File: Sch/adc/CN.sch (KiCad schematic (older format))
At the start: 20 parts, among them J1 JP4, J2 Header5, P1 CONN_02X40, U1 LTC2292

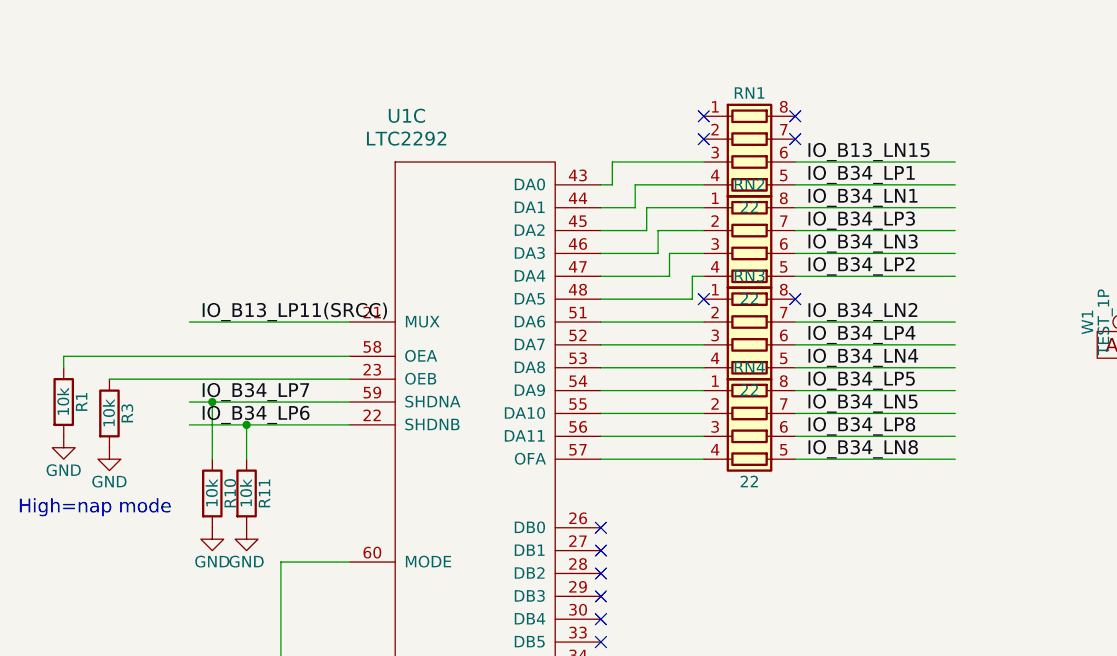
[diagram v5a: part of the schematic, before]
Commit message: Fix RA footprint
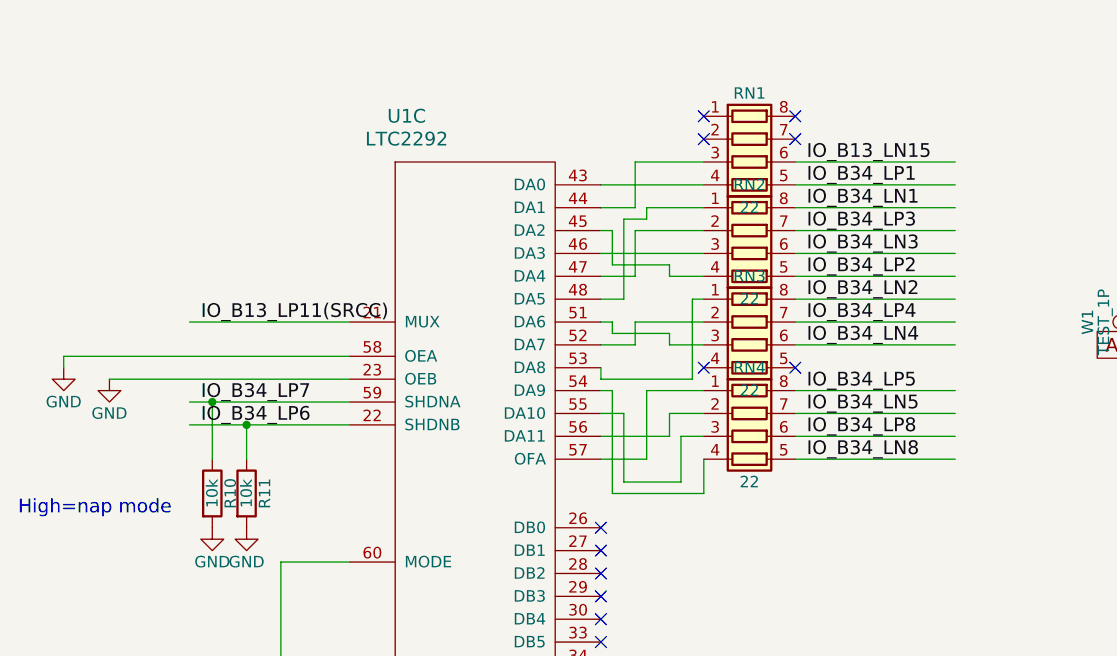
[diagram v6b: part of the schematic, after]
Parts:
- removed R1, R3: 10k, adc_lib:R0603, symbol R
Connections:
- wire segments 125 -> 145
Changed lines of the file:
@@
 Text Label 4200 3050 0    60   ~ 0
 IO_B34_LN8
-Text Label 4200 2650 0    60   ~ 0
+Text Label 4200 2550 0    60   ~ 0
 IO_B34_LN4
-Text Label 4200 2550 0    60   ~ 0
+Text Label 4200 2450 0    60   ~ 0
 IO_B34_LP4
-Text Label 4200 2450 0    60   ~ 0
+Text Label 4200 2350 0    60   ~ 0
 IO_B34_LN2
 Text Label 4200 2250 0    60   ~ 0
@@
 L GND #PWR010
 U 1 1 58A86709
-P 950 2950
-F 0 "#PWR010" H 950 2700 50  0001 C CNN
-F 1 "GND" H 950 2800 50  0000 C CNN
-F 2 "" H 950 2950 50  0000 C CNN
-F 3 "" H 950 2950 50  0000 C CNN
-	1    950  2950
-	1    0    0    -1
-$EndComp
-$Comp
-L R R1
-U 1 1 58A86735
-P 950 2800
-F 0 "R1" V 1030 2800 50  0000 C CNN
-F 1 "10k" V 950 2800 50  0000 C CNN
-F 2 "adc_lib:R0603" V 880 2800 50  0001 C CNN
-F 3 "" H 950 2800 50  0000 C CNN
-	1    950  2800
+P 950 2650
+F 0 "#PWR010" H 950 2400 50  0001 C CNN
+F 1 "GND" H 950 2500 50  0000 C CNN
+F 2 "" H 950 2650 50  0000 C CNN
+F 3 "" H 950 2650 50  0000 C CNN
+	1    950  2650
 	1    0    0    -1
 $EndComp
@@
 	4850 2250 4150 2250
 Wire Wire Line
+	4850 2350 4150 2350
+Wire Wire Line
 	4850 2450 4150 2450
 Wire Wire Line
 	4850 2550 4150 2550
-Wire Wire Line
-	4850 2650 4150 2650
 Wire Wire Line
 	4150 1850 4850 1850
@@
 Wire Wire Line
 	7150 2250 8150 2250
-Wire Wire Line
-	3300 2450 3750 2450
-Wire Wire Line
-	3300 2550 3750 2550
-Wire Wire Line
-	3300 2650 3750 2650
-Wire Wire Line
-	3300 2750 3750 2750
-Wire Wire Line
-	3300 2850 3750 2850
-Wire Wire Line
-	3300 2950 3750 2950
-Wire Wire Line
-	3300 3050 3750 3050
 Wire Wire Line
 	1500 2900 2200 2900
@@
 	1    0    0    -1
 $EndComp
-Wire Wire Line
-	3300 2350 3700 2350
-Wire Wire Line
-	3700 2350 3700 2250
-Wire Wire Line
-	3700 2250 3750 2250
-Wire Wire Line
-	3300 2250 3600 2250
-Wire Wire Line
-	3600 2250 3600 2150
-Wire Wire Line
-	3600 2150 3750 2150
-NoConn ~ 3750 2350
-Wire Wire Line
-	3300 2150 3550 2150
-Wire Wire Line
-	3550 2150 3550 2050
-Wire Wire Line
-	3550 2050 3750 2050
-Wire Wire Line
-	3300 2050 3500 2050
-Wire Wire Line
-	3500 2050 3500 1950
-Wire Wire Line
-	3500 1950 3750 1950
-Wire Wire Line
-	3300 1950 3450 1950
-Wire Wire Line
-	3450 1950 3450 1850
-Wire Wire Line
-	3450 1850 3750 1850
-Wire Wire Line
-	3300 1850 3350 1850
-Wire Wire Line
-	3350 1850 3350 1750
-Wire Wire Line
-	3350 1750 3750 1750
-NoConn ~ 4150 2350
 NoConn ~ 4150 1550
 NoConn ~ 4150 1650
 $Comp
-L R R3
-U 1 1 58B07F2F
-P 1150 2850
-F 0 "R3" V 1230 2850 50  0000 C CNN
-F 1 "10k" V 1150 2850 50  0000 C CNN
-F 2 "adc_lib:R0603" V 1080 2850 50  0001 C CNN
-F 3 "" H 1150 2850 50  0000 C CNN
-	1    1150 2850
-	1    0    0    -1
-$EndComp
-$Comp
 L GND #PWR014
 U 1 1 58B07F94
-P 1150 3000
-F 0 "#PWR014" H 1150 2750 50  0001 C CNN
-F 1 "GND" H 1150 2850 50  0000 C CNN
-F 2 "" H 1150 3000 50  0000 C CNN
-F 3 "" H 1150 3000 50  0000 C CNN
-	1    1150 3000
-	1    0    0    -1
-$EndComp
+P 1150 2700
+F 0 "#PWR014" H 1150 2450 50  0001 C CNN
+F 1 "GND" H 1150 2550 50  0000 C CNN
+F 2 "" H 1150 2700 50  0000 C CNN
+F 3 "" H 1150 2700 50  0000 C CNN
+	1    1150 2700
+	1    0    0    -1
+$EndComp
+Wire Wire Line
+	3300 3050 3500 3050
+Wire Wire Line
+	3500 3050 3500 2750
+Wire Wire Line
+	3500 2750 3750 2750
+Wire Wire Line
+	3300 2950 3600 2950
+Wire Wire Line
+	3600 2950 3600 2850
+Wire Wire Line
+	3600 2850 3750 2850
+Wire Wire Line
+	3300 2850 3400 2850
+Wire Wire Line
+	3400 2850 3400 3150
+Wire Wire Line
+	3400 3150 3650 3150
+Wire Wire Line
+	3650 3150 3650 2950
+Wire Wire Line
+	3650 2950 3750 2950
+Wire Wire Line
+	3300 2750 3350 2750
+Wire Wire Line
+	3350 2750 3350 3200
+Wire Wire Line
+	3350 3200 3750 3200
+Wire Wire Line
+	3750 3200 3750 3050
+Wire Wire Line
+	3750 2350 3700 2350
+Wire Wire Line
+	3700 2350 3700 2700
+Wire Wire Line
+	3700 2700 3300 2700
+Wire Wire Line
+	3300 2700 3300 2650
+Wire Wire Line
+	3300 2550 3450 2550
+Wire Wire Line
+	3450 2550 3450 2450
+Wire Wire Line
+	3450 2450 3750 2450
+Wire Wire Line
+	3300 2450 3350 2450
+Wire Wire Line
+	3350 2450 3350 2500
+Wire Wire Line
+	3350 2500 3600 2500
+Wire Wire Line
+	3600 2500 3600 2550
+Wire Wire Line
+	3600 2550 3750 2550
+NoConn ~ 3750 2650
+NoConn ~ 4150 2650
+Wire Wire Line
+	3300 2350 3400 2350
+Wire Wire Line
+	3400 2350 3400 2000
+Wire Wire Line
+	3400 2000 3500 2000
+Wire Wire Line
+	3500 2000 3500 1950
+Wire Wire Line
+	3500 1950 3750 1950
+Wire Wire Line
+	3300 2250 3450 2250
+Wire Wire Line
+	3450 2250 3450 2050
+Wire Wire Line
+	3450 2050 3750 2050
+Wire Wire Line
+	3300 2150 3750 2150
+Wire Wire Line
+	3300 2050 3350 2050
+Wire Wire Line
+	3350 2050 3350 2200
+Wire Wire Line
+	3350 2200 3600 2200
+Wire Wire Line
+	3600 2200 3600 2250
+Wire Wire Line
+	3600 2250 3750 2250
+Wire Wire Line
+	3300 1850 3750 1850
+Wire Wire Line
+	3300 1950 3450 1950
+Wire Wire Line
+	3450 1950 3450 1750
+Wire Wire Line
+	3450 1750 3750 1750
 $EndSCHEMATC

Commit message: Add routing
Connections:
- wire segments 145 -> 146
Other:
- moved on the sheet: RN5
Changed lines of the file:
@@
 IO_B13_LP11(SRCC)
 Text Label 4200 2750 0    60   ~ 0
-IO_B34_LP5
+IO_B13_LN11
 Text Label 4200 2850 0    60   ~ 0
-IO_B34_LN5
+IO_B13_LP12(MRCC)
 Text Label 4200 2950 0    60   ~ 0
-IO_B34_LP8
+IO_B13_LP21
 Text Label 4200 3050 0    60   ~ 0
-IO_B34_LN8
+IO_B13_LN21
 Text Label 4200 2550 0    60   ~ 0
-IO_B34_LN4
+IO_B34_LP1
 Text Label 4200 2450 0    60   ~ 0
-IO_B34_LP4
+IO_B13_LN15
 Text Label 4200 2350 0    60   ~ 0
 IO_B34_LN2
 Text Label 4200 2250 0    60   ~ 0
-IO_B34_LP2
+IO_B34_LN3
 Text Label 4200 1850 0    60   ~ 0
-IO_B34_LP1
+IO_B34_LN4
 Text Label 4200 1950 0    60   ~ 0
 IO_B34_LN1
@@
 IO_B34_LP3
 Text Label 4200 2150 0    60   ~ 0
-IO_B34_LN3
+IO_B34_LP2
 Text Label 4200 1750 0    60   ~ 0
-IO_B13_LN15
+IO_B34_LP4
 Text Label 1550 2800 0    60   ~ 0
 IO_B34_LP7
 Text Label 1550 2900 0    60   ~ 0
-IO_B34_LP6
+IO_B13_LN14
 NoConn ~ 5950 3950
 Text Notes 5100 800  0    60   ~ 0
@@
 	1    0    0    -1
 $EndComp
-NoConn ~ 7850 2450
 NoConn ~ 5950 1950
 NoConn ~ 5950 2350
 NoConn ~ 5950 2650
 NoConn ~ 5950 2750
-Text GLabel 5950 2550 0    60   Input ~ 0
+Text GLabel 7850 2450 2    60   Input ~ 0
 ADC_CLK
 $Comp
@@
 	6650 3350 5950 3350
 Wire Wire Line
-	6650 3550 5950 3550
+	5100 3550 6650 3550
 Wire Wire Line
 	6650 3650 5950 3650
 Wire Wire Line
-	6650 3750 5950 3750
-Wire Wire Line
-	6650 3850 5950 3850
+	5100 3750 6650 3750
+Wire Wire Line
+	5100 3850 6650 3850
 Wire Wire Line
 	6650 3950 5950 3950
@@
 	7150 2450 7850 2450
 Wire Wire Line
-	7150 2550 8650 2550
-Wire Wire Line
-	7150 2650 8650 2650
-Wire Wire Line
-	7150 2750 8650 2750
+	7150 2650 8350 2650
 Wire Wire Line
 	7150 2950 7850 2950
@@
 Text Notes 750  3300 0    60   ~ 0
 High=nap mode
-Text GLabel 9050 2550 2    60   Output ~ 0
+Text GLabel 4700 3650 0    60   Output ~ 0
 FS
-Text GLabel 9050 2650 2    60   Output ~ 0
+Text GLabel 4700 3750 0    60   Output ~ 0
 BCLK
-Text GLabel 9050 2750 2    60   Output ~ 0
+Text GLabel 4700 3850 0    60   Output ~ 0
 DACIN
 Text GLabel 5650 4050 0    60   Output ~ 0
 MCLK
-Text GLabel 5950 2150 0    60   BiDi ~ 0
+Text GLabel 7850 3550 2    60   BiDi ~ 0
 SCL
-Text GLabel 5950 2250 0    60   BiDi ~ 0
+Text GLabel 7850 3450 2    60   BiDi ~ 0
 SDA
 $Comp
 L R_Pack04 RN5
 U 1 1 58A9A1DD
-P 8850 2650
-F 0 "RN5" V 8550 2650 50  0000 C CNN
-F 1 "22" V 9050 2650 50  0000 C CNN
-F 2 "adc_lib:EXB-38V220JV" V 9125 2650 50  0001 C CNN
-F 3 "" H 8850 2650 50  0000 C CNN
-	1    8850 2650
-	0    1    1    0
-$EndComp
-NoConn ~ 8650 2450
-NoConn ~ 9050 2450
+P 4900 3850
+F 0 "RN5" V 4600 3850 50  0000 C CNN
+F 1 "22" V 5100 3850 50  0000 C CNN
+F 2 "adc_lib:EXB-38V220JV" V 5175 3850 50  0001 C CNN
+F 3 "" H 4900 3850 50  0000 C CNN
+	1    4900 3850
+	0    -1   1    0
+$EndComp
 $Comp
 L R R12
@@
 Wire Wire Line
 	3450 1750 3750 1750
+Wire Wire Line
+	7150 2750 8350 2750
+Wire Wire Line
+	7150 2550 8350 2550
+Wire Wire Line
+	5100 3550 5100 3650
+NoConn ~ 4700 3950
+NoConn ~ 5100 3950
+NoConn ~ 5950 2550
 $EndSCHEMATC

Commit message: layout more
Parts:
- added R1: 22, adc_lib:R0603, symbol R
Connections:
- net labels added: MUX, SHDNA, SHDNB
- net labels removed: IO_B34_LN7, IO_B34_LP7
- wire segments 146 -> 147
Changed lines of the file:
@@
 IO_B34_LN5
 Text Label 7200 3650 0    60   ~ 0
-IO_B34_LP7
+SHDNA
 Text Label 7200 3750 0    60   ~ 0
-IO_B34_LN7
+SHDNB
 Text Label 6000 4050 0    60   ~ 0
 IO_B34_LN11
@@
 IO_B13_LP11(SRCC)
 Text Label 4200 2750 0    60   ~ 0
-IO_B13_LN11
+IO_B13_LP21
 Text Label 4200 2850 0    60   ~ 0
-IO_B13_LP12(MRCC)
+IO_B13_LN13
 Text Label 4200 2950 0    60   ~ 0
-IO_B13_LP21
+IO_B13_LP15
 Text Label 4200 3050 0    60   ~ 0
 IO_B13_LN21
 Text Label 4200 2550 0    60   ~ 0
-IO_B34_LP1
+IO_B34_LN1
 Text Label 4200 2450 0    60   ~ 0
 IO_B13_LN15
 Text Label 4200 2350 0    60   ~ 0
-IO_B34_LN2
+IO_B34_LP1
 Text Label 4200 2250 0    60   ~ 0
 IO_B34_LN3
@@
 IO_B34_LN4
 Text Label 4200 1950 0    60   ~ 0
-IO_B34_LN1
+IO_B34_LP2
 Text Label 4200 2050 0    60   ~ 0
 IO_B34_LP3
 Text Label 4200 2150 0    60   ~ 0
-IO_B34_LP2
+IO_B34_LN2
 Text Label 4200 1750 0    60   ~ 0
 IO_B34_LP4
 Text Label 1550 2800 0    60   ~ 0
-IO_B34_LP7
+SHDNA
 Text Label 1550 2900 0    60   ~ 0
-IO_B13_LN14
+SHDNB
 NoConn ~ 5950 3950
 Text Notes 5100 800  0    60   ~ 0
@@
 NoConn ~ 7150 5550
 NoConn ~ 6650 5650
-Text Label 1550 2450 0    60   ~ 0
-IO_B13_LP11(SRCC)
 $Comp
 L R R24
@@
 $EndComp
 NoConn ~ 5950 1950
-NoConn ~ 5950 2350
-NoConn ~ 5950 2650
-NoConn ~ 5950 2750
 Text GLabel 7850 2450 2    60   Input ~ 0
 ADC_CLK
@@
 LED
 NoConn ~ 5950 3650
-NoConn ~ 7850 3750
 Text Notes 3700 7150 0    60   ~ 0
 MODE, Output Format, Clock Duty Cycle Stabilizer\n0, Offset Binary, Off\n1/3Vdd, Offset Binary, On\n2/3Vdd, 2's complement, On\nVdd, 2's complement, Off
@@
 NoConn ~ 4700 3950
 NoConn ~ 5100 3950
+NoConn ~ 5950 2250
+NoConn ~ 5950 2150
+$Comp
+L R R1
+U 1 1 58B3E1F0
+P 5800 2350
+F 0 "R1" V 5880 2350 50  0000 C CNN
+F 1 "22" V 5800 2350 50  0000 C CNN
+F 2 "adc_lib:R0603" V 5730 2350 50  0001 C CNN
+F 3 "" H 5800 2350 50  0000 C CNN
+	1    5800 2350
+	0    1    1    0
+$EndComp
+Wire Wire Line
+	5650 2350 5200 2350
+Text Label 5300 2350 0    60   ~ 0
+MUX
+Text Label 1700 2450 0    60   ~ 0
+MUX
+NoConn ~ 5950 2050
+NoConn ~ 8350 2550
 NoConn ~ 5950 2550
 $EndSCHEMATC
